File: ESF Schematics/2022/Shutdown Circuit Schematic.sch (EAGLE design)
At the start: 69 parts, among them J1 CONNECTOR-1_LCAX2-14F-E, J2 CONNECTOR-1_LCAX2-14F-E, J3 CONNECTOR-1_LCAX2-14F-E, J4 CONNECTOR-1_LCAX2-14F-E

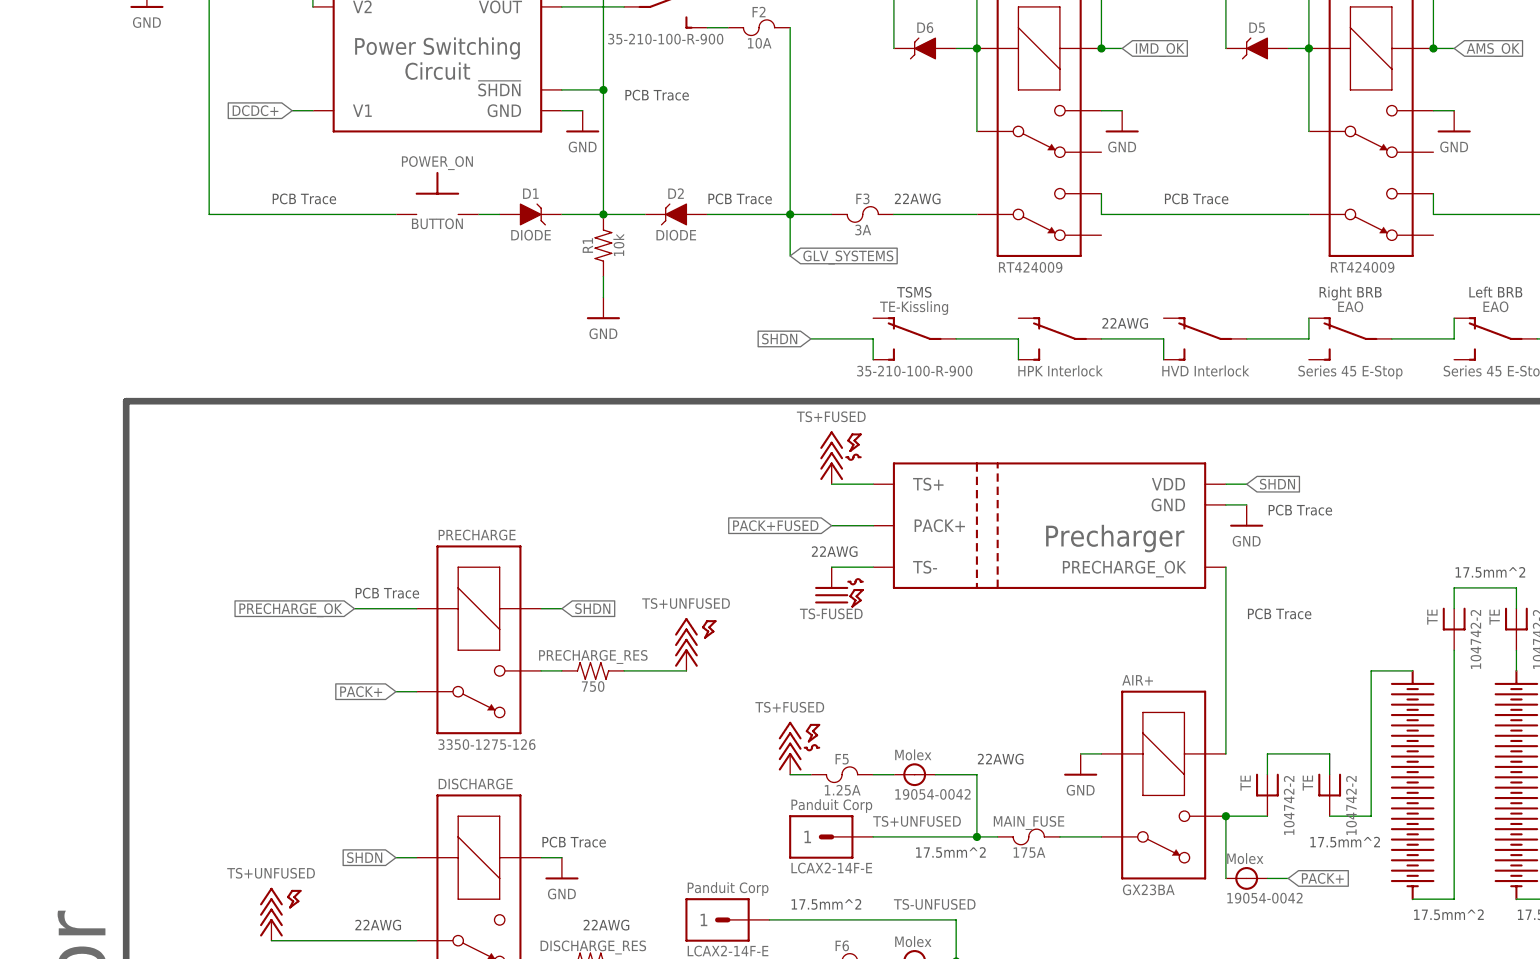
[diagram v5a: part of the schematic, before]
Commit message: updated all schem to comply with ESF comments
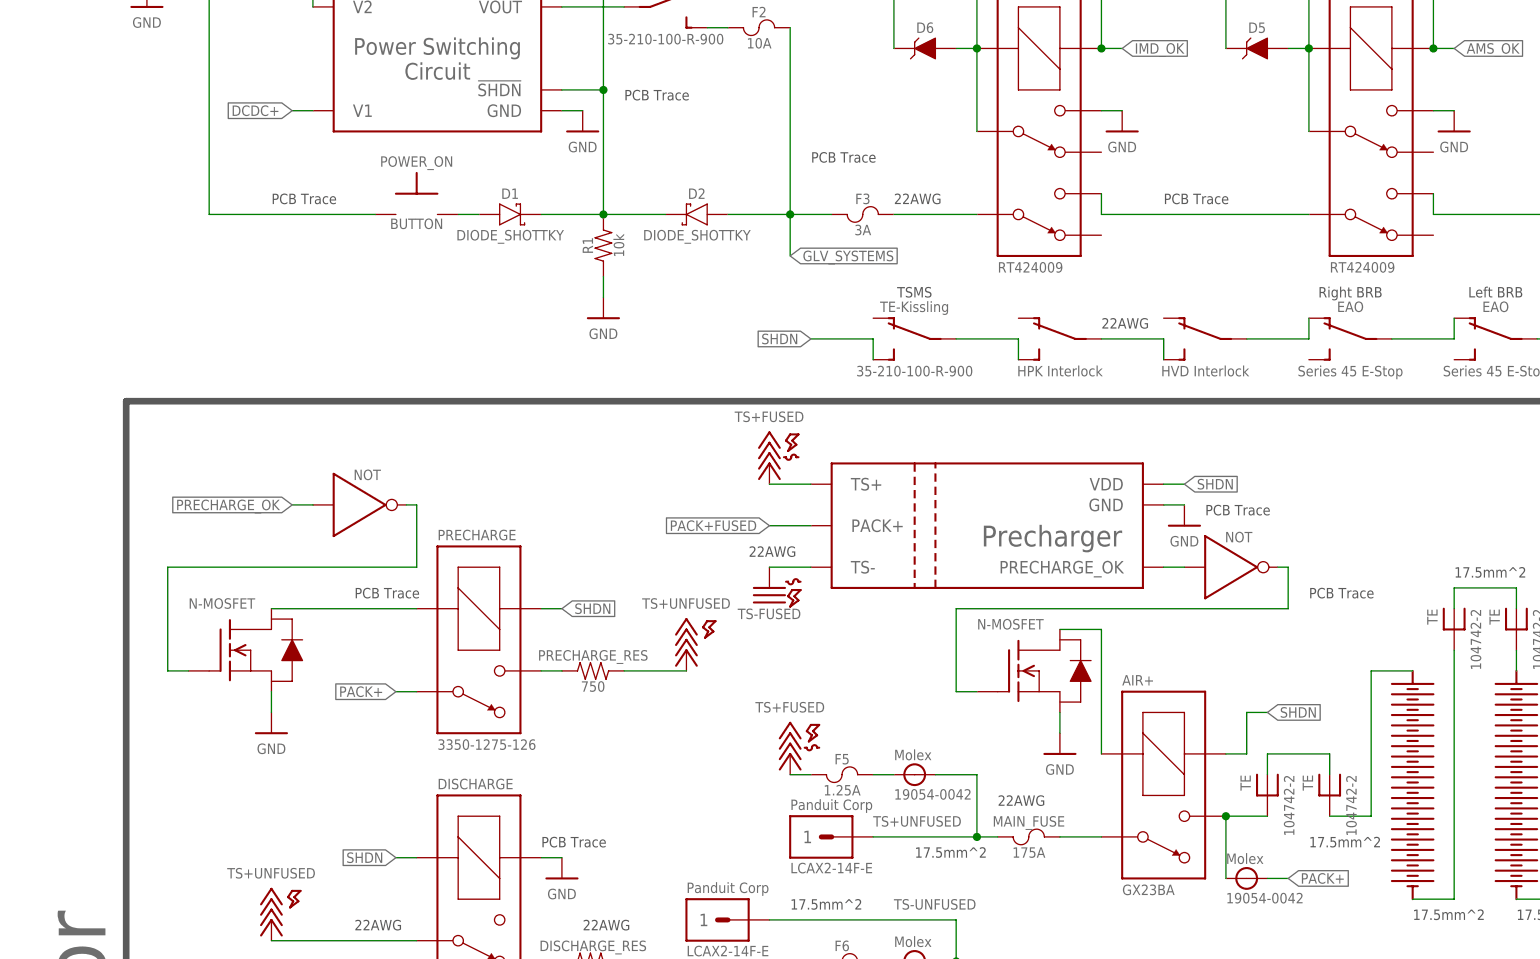
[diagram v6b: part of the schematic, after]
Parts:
- added Q1, Q2: MOSFET_N-CHANNEL, HyTechSymbolsTemp:MOSFET_N-CHANNEL
- added U1, U2: LOGICGATE_INVERTER, HyTechSymbolsTemp:LOGICGATE_INVERTER
- D1, D2: value DIODE -> DIODE_SHOTTKY; device HyTechSymbolsTemp:DIODE -> HyTechSymbolsTemp:DIODE_SHOTTKY
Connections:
- removed net RELAY_CTRL: AIR+.COIL-, U$17.PRECHARGE_OK
- new net N$24: Q1.G, U1.!IN
- new net N$25: U$17.PRECHARGE_OK, U2.IN
- new net N$52: Q2.G, U2.!IN
- new net N$53: AIR+.COIL+, Q2.D
- net GND: now also Q1.S, Q2.S; no longer AIR+.COIL+
- net PRECHARGE_OK: now also Q1.D, U1.IN
- net SHDN: now also AIR+.COIL-
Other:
- moved on the sheet: POWER_ON

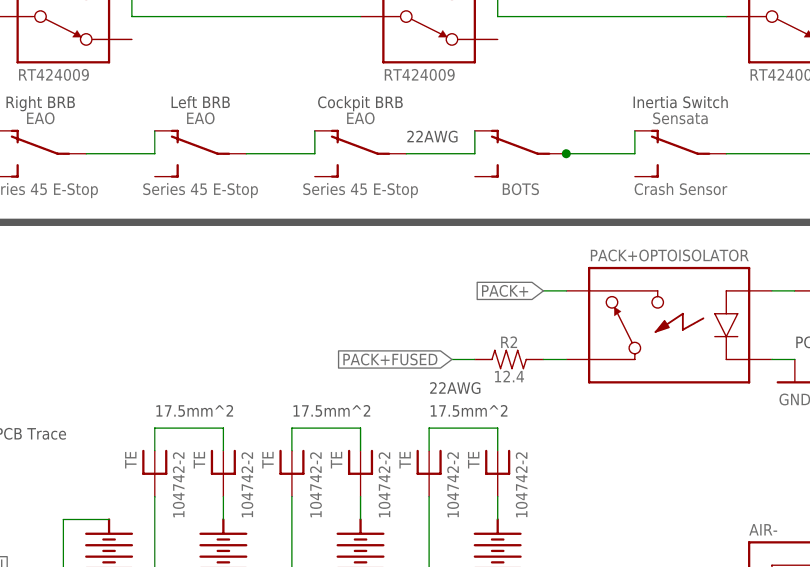
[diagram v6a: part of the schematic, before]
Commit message: revised schematics to reflect most accurate information
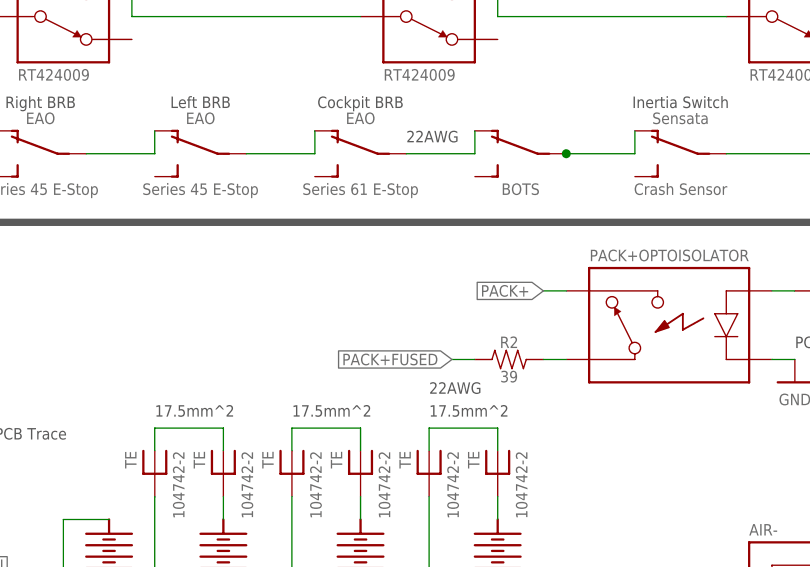
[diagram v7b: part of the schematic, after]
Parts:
- R2: value 12.4 -> 39
- S3: value SWITCH_SPST_34MM_STOP -> SWITCH_SPST_27MM_STOP; device HyTechSymbols:SWITCH_SPST_34MM_STOP -> HyTechSymbols:SWITCH_SPST_27MM_STOP
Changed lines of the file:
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@@
 <part name="PACK+OPTOISOLATOR" library="HyTechSymbolsTemp" deviceset="RELAY_SOLIDSTATE_NO_*" device=""/>
 <part name="P18" library="HyTechSupplies" deviceset="GND" device=""/>
-<part name="R2" library="HyTechSymbolsTemp" deviceset="RESISTOR" device="" value="12.4"/>
+<part name="R2" library="HyTechSymbolsTemp" deviceset="RESISTOR" device="" value="39"/>
 <part name="R3" library="HyTechSymbolsTemp" deviceset="RESISTOR" device="" value="1k"/>
 <part name="S1" library="HyTechSymbols" deviceset="SWITCH_SPST_*" device="" technology="INERTIA_SWITCH"/>
@@
 <attribute name="MPN" value="BOTS"/>
 </part>
-<part name="S3" library="HyTechSymbols" deviceset="SWITCH_SPST_*" device="" technology="34MM_STOP"/>
+<part name="S3" library="HyTechSymbols" deviceset="SWITCH_SPST_*" device="" technology="27MM_STOP" value="SWITCH_SPST_27MM_STOP"/>
 <part name="S4" library="HyTechSymbols" deviceset="SWITCH_SPST_*" device="" technology="40MM_STOP"/>
 <part name="S5" library="HyTechSymbols" deviceset="SWITCH_SPST_*" device="" technology="40MM_STOP"/>
